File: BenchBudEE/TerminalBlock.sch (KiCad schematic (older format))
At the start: 2 parts, among them P4 12 pin terminal block, P5 3 Pin TB

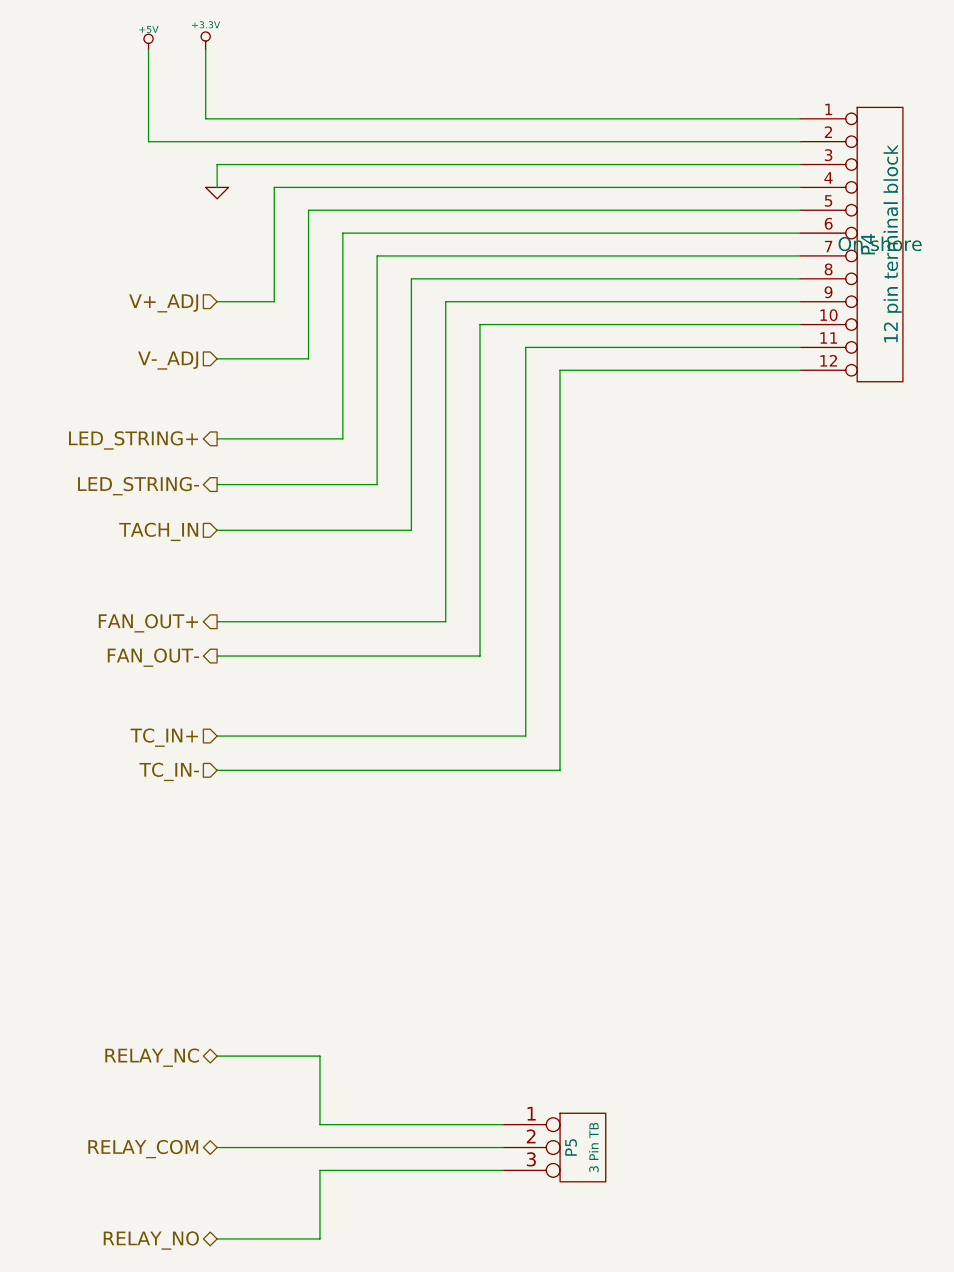
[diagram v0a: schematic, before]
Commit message: Ground and Power Planes
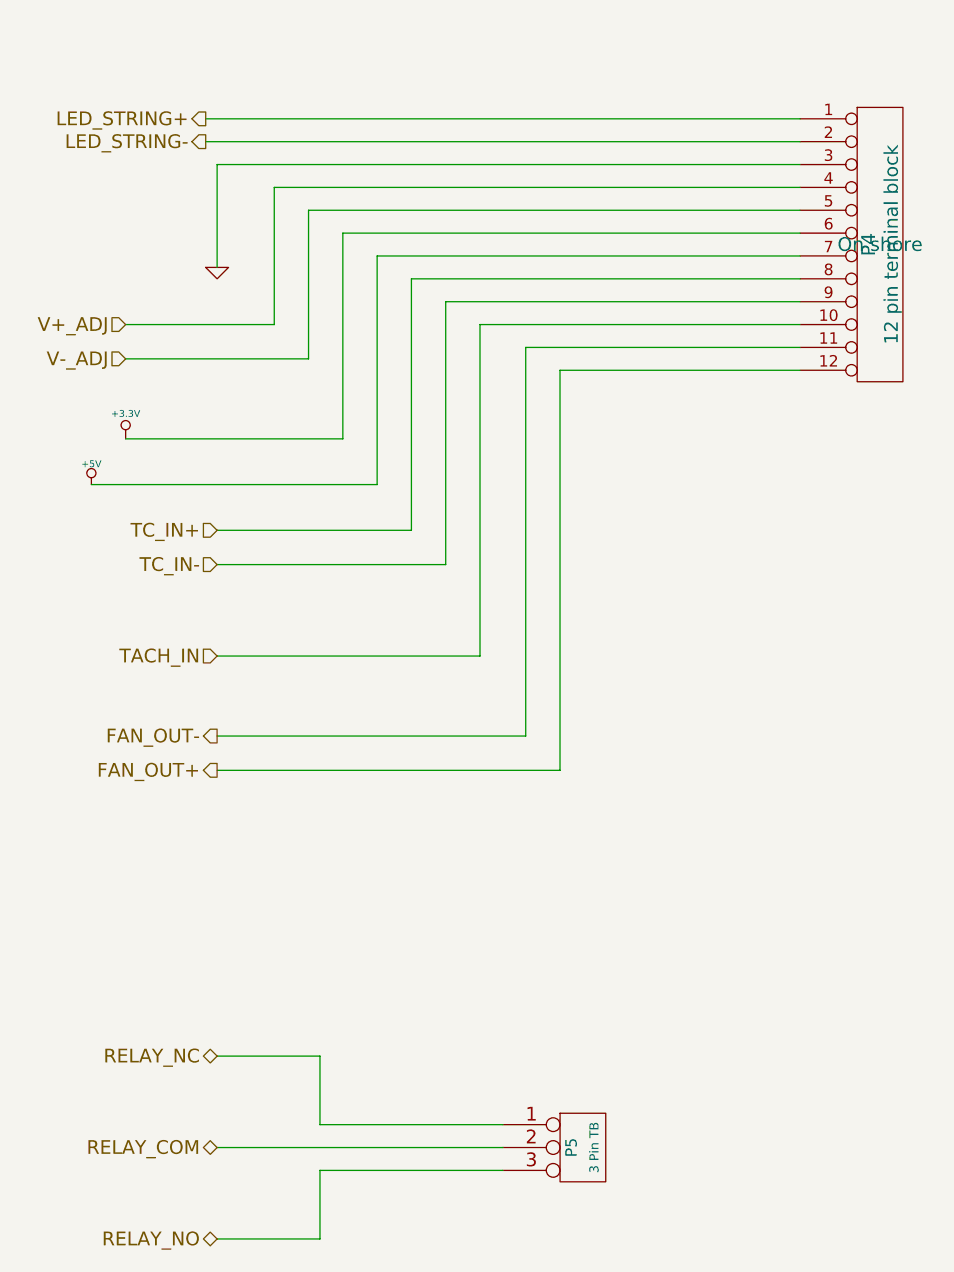
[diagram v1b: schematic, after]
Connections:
- net +3.3V: now also P4.6 (P6); no longer P4.1 (P1)
- net +5V: now also P4.7 (P7); no longer P4.2 (P2)
- net FAN_OUT+: now also P4.12 (P12); no longer P4.9 (P9)
- net FAN_OUT-: now also P4.11 (P11); no longer P4.10 (P10)
- net LED_STRING+: now also P4.1 (P1); no longer P4.6 (P6)
- net LED_STRING-: now also P4.2 (P2); no longer P4.7 (P7)
- net TACH_IN: now also P4.10 (P10); no longer P4.8 (P8)
- net TC_IN+: now also P4.8 (P8); no longer P4.11 (P11)
- net TC_IN-: now also P4.9 (P9); no longer P4.12 (P12)
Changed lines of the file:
@@
 Sheet 6 9
 Title ""
-Date "27 feb 2014"
+Date "1 mar 2014"
 Rev ""
 Comp ""
@@
 Comment4 ""
 $EndDescr
-Text HLabel 1850 1800 0    60   Input ~ 0
+Text HLabel 1450 1900 0    60   Input ~ 0
 V+_ADJ
-Text HLabel 1850 2050 0    60   Input ~ 0
+Text HLabel 1450 2050 0    60   Input ~ 0
 V-_ADJ
+Text HLabel 1850 3350 0    60   Input ~ 0
+TACH_IN
+Text HLabel 1800 1000 0    60   Output ~ 0
+LED_STRING+
+Text HLabel 1800 1100 0    60   Output ~ 0
+LED_STRING-
 Text HLabel 1850 2800 0    60   Input ~ 0
-TACH_IN
-Text HLabel 1850 2400 0    60   Output ~ 0
-LED_STRING+
-Text HLabel 1850 2600 0    60   Output ~ 0
-LED_STRING-
-Text HLabel 1850 3700 0    60   Input ~ 0
 TC_IN+
-Text HLabel 1850 3850 0    60   Input ~ 0
+Text HLabel 1850 2950 0    60   Input ~ 0
 TC_IN-
 Text HLabel 1850 5500 0    60   BiDi ~ 0
@@
 Text HLabel 1850 5900 0    60   BiDi ~ 0
 RELAY_NO
-Text HLabel 1850 3200 0    60   Output ~ 0
+Text HLabel 1850 3850 0    60   Output ~ 0
 FAN_OUT+
-Text HLabel 1850 3350 0    60   Output ~ 0
+Text HLabel 1850 3700 0    60   Output ~ 0
 FAN_OUT-
 $Comp
-L +3.3V #PWR038
+L +3.3V #PWR41
 U 1 1 52F7DDCB
-P 1800 700
-F 0 "#PWR038" H 1800 660 30  0001 C CNN
-F 1 "+3.3V" H 1800 810 30  0000 C CNN
-F 2 "" H 1800 700 60  0000 C CNN
-F 3 "" H 1800 700 60  0000 C CNN
-	1    1800 700
+P 1450 2400
+F 0 "#PWR41" H 1450 2360 30  0001 C CNN
+F 1 "+3.3V" H 1450 2510 30  0000 C CNN
+F 2 "" H 1450 2400 60  0000 C CNN
+F 3 "" H 1450 2400 60  0000 C CNN
+	1    1450 2400
 	1    0    0    -1
 $EndComp
 $Comp
-L +5V #PWR039
+L +5V #PWR40
 U 1 1 52F7DDDA
-P 1550 700
-F 0 "#PWR039" H 1550 790 20  0001 C CNN
-F 1 "+5V" H 1550 790 30  0000 C CNN
-F 2 "" H 1550 700 60  0000 C CNN
-F 3 "" H 1550 700 60  0000 C CNN
-	1    1550 700
+P 1300 2600
+F 0 "#PWR40" H 1300 2690 20  0001 C CNN
+F 1 "+5V" H 1300 2690 30  0000 C CNN
+F 2 "" H 1300 2600 60  0000 C CNN
+F 3 "" H 1300 2600 60  0000 C CNN
+	1    1300 2600
 	1    0    0    -1
 $EndComp
 $Comp
-L GND #PWR040
+L GND #PWR42
 U 1 1 52F7DDE9
-P 1850 1300
-F 0 "#PWR040" H 1850 1300 30  0001 C CNN
-F 1 "GND" H 1850 1230 30  0001 C CNN
-F 2 "" H 1850 1300 60  0000 C CNN
-F 3 "" H 1850 1300 60  0000 C CNN
-	1    1850 1300
+P 1850 1650
+F 0 "#PWR42" H 1850 1650 30  0001 C CNN
+F 1 "GND" H 1850 1580 30  0001 C CNN
+F 2 "" H 1850 1650 60  0000 C CNN
+F 3 "" H 1850 1650 60  0000 C CNN
+	1    1850 1650
 	1    0    0    -1
 $EndComp
@@
 	4400 1000 1800 1000
 Wire Wire Line
-	1800 1000 1800 700
+	1800 1100 4400 1100
 Wire Wire Line
-	1550 700  1550 1100
-Wire Wire Line
-	1550 1100 4400 1100
-Wire Wire Line
-	1850 1300 1850 1200
+	1850 1650 1850 1200
 Wire Wire Line
 	1850 1200 4400 1200
 Wire Wire Line
-	1850 1800 2100 1800
-Wire Wire Line
-	2100 1800 2100 1300
+	2100 1300 2100 1900
 Wire Wire Line
 	2100 1300 4400 1300
@@
 	2250 1400 2250 2050
 Wire Wire Line
-	2250 2050 1850 2050
-Wire Wire Line
-	1850 2400 2400 2400
+	1450 2400 2400 2400
 Wire Wire Line
 	2400 2400 2400 1500
@@
 	2550 1600 2550 2600
 Wire Wire Line
-	2550 2600 1850 2600
+	2550 2600 1300 2600
 Wire Wire Line
 	1850 2800 2700 2800
@@
 	2700 1700 4400 1700
 Wire Wire Line
-	1850 3200 2850 3200
-Wire Wire Line
-	2850 3200 2850 1800
+	2850 2950 2850 1800
 Wire Wire Line
 	2850 1800 4400 1800
@@
 Wire Wire Line
 	2300 5600 3100 5600
+Wire Wire Line
+	1850 2950 2850 2950
+Wire Wire Line
+	2100 1900 1450 1900
+Wire Wire Line
+	2250 2050 1450 2050
 $EndSCHEMATC

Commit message: Reality Check
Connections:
- net RELAY_NC: now also P5.3 (P3); no longer P5.1 (P1)
- net RELAY_NO: now also P5.1 (P1); no longer P5.3 (P3)
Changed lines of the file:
@@
 Text HLabel 1850 5500 0    60   BiDi ~ 0
 RELAY_COM
+Text HLabel 1850 5900 0    60   BiDi ~ 0
+RELAY_NC
 Text HLabel 1850 5100 0    60   BiDi ~ 0
-RELAY_NC
-Text HLabel 1850 5900 0    60   BiDi ~ 0
 RELAY_NO
 Text HLabel 1850 3850 0    60   Output ~ 0

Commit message: Layout Work Session 4
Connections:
- net +3.3V: now also P4.10 (P10); no longer P4.6 (P6)
- net +5V: now also P4.9 (P9); no longer P4.7 (P7)
- net FAN_OUT+: now also P4.5 (P5); no longer P4.12 (P12)
- net FAN_OUT-: now also P4.4 (P4); no longer P4.11 (P11)
- net GND: now also P4.8 (P8); no longer P4.3 (P3)
- net TACH_IN: now also P4.3 (P3); no longer P4.10 (P10)
- net TC_IN+: now also P4.7 (P7); no longer P4.8 (P8)
- net TC_IN-: now also P4.6 (P6); no longer P4.9 (P9)
- net V+_ADJ: now also P4.12 (P12); no longer P4.4 (P4)
- net V-_ADJ: now also P4.11 (P11); no longer P4.5 (P5)
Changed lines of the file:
@@
 Sheet 6 9
 Title ""
-Date "1 mar 2014"
+Date "2 mar 2014"
 Rev ""
 Comp ""
@@
 Comment4 ""
 $EndDescr
-Text HLabel 1450 1900 0    60   Input ~ 0
+Text HLabel 1850 3850 0    60   Input ~ 0
 V+_ADJ
-Text HLabel 1450 2050 0    60   Input ~ 0
+Text HLabel 1850 3700 0    60   Input ~ 0
 V-_ADJ
-Text HLabel 1850 3350 0    60   Input ~ 0
+Text HLabel 1850 1650 0    60   Input ~ 0
 TACH_IN
-Text HLabel 1800 1000 0    60   Output ~ 0
+Text HLabel 1850 1000 0    60   Output ~ 0
 LED_STRING+
-Text HLabel 1800 1100 0    60   Output ~ 0
+Text HLabel 1850 1100 0    60   Output ~ 0
 LED_STRING-
-Text HLabel 1850 2800 0    60   Input ~ 0
+Text HLabel 1850 2450 0    60   Input ~ 0
 TC_IN+
-Text HLabel 1850 2950 0    60   Input ~ 0
+Text HLabel 1850 2300 0    60   Input ~ 0
 TC_IN-
 Text HLabel 1850 5500 0    60   BiDi ~ 0
@@
 Text HLabel 1850 5100 0    60   BiDi ~ 0
 RELAY_NO
-Text HLabel 1850 3850 0    60   Output ~ 0
+Text HLabel 1850 2050 0    60   Output ~ 0
 FAN_OUT+
-Text HLabel 1850 3700 0    60   Output ~ 0
+Text HLabel 1850 1850 0    60   Output ~ 0
 FAN_OUT-
 $Comp
 L +3.3V #PWR034
 U 1 1 52F7DDCB
-P 1450 2400
-F 0 "#PWR034" H 1450 2360 30  0001 C CNN
-F 1 "+3.3V" H 1450 2510 30  0000 C CNN
-F 2 "" H 1450 2400 60  0000 C CNN
-F 3 "" H 1450 2400 60  0000 C CNN
-	1    1450 2400
+P 1400 3300
+F 0 "#PWR034" H 1400 3260 30  0001 C CNN
+F 1 "+3.3V" H 1400 3410 30  0000 C CNN
+F 2 "" H 1400 3300 60  0000 C CNN
+F 3 "" H 1400 3300 60  0000 C CNN
+	1    1400 3300
 	1    0    0    -1
 $EndComp
@@
 L +5V #PWR035
 U 1 1 52F7DDDA
-P 1300 2600
-F 0 "#PWR035" H 1300 2690 20  0001 C CNN
-F 1 "+5V" H 1300 2690 30  0000 C CNN
-F 2 "" H 1300 2600 60  0000 C CNN
-F 3 "" H 1300 2600 60  0000 C CNN
-	1    1300 2600
+P 1550 3050
+F 0 "#PWR035" H 1550 3140 20  0001 C CNN
+F 1 "+5V" H 1550 3140 30  0000 C CNN
+F 2 "" H 1550 3050 60  0000 C CNN
+F 3 "" H 1550 3050 60  0000 C CNN
+	1    1550 3050
 	1    0    0    -1
 $EndComp
@@
 L GND #PWR036
 U 1 1 52F7DDE9
-P 1850 1650
-F 0 "#PWR036" H 1850 1650 30  0001 C CNN
-F 1 "GND" H 1850 1580 30  0001 C CNN
-F 2 "" H 1850 1650 60  0000 C CNN
-F 3 "" H 1850 1650 60  0000 C CNN
-	1    1850 1650
+P 1850 2800
+F 0 "#PWR036" H 1850 2800 30  0001 C CNN
+F 1 "GND" H 1850 2730 30  0001 C CNN
+F 2 "" H 1850 2800 60  0000 C CNN
+F 3 "" H 1850 2800 60  0000 C CNN
+	1    1850 2800
 	1    0    0    -1
 $EndComp
@@
 $EndComp
 Wire Wire Line
-	4400 1000 1800 1000
+	4400 1000 1850 1000
 Wire Wire Line
-	1800 1100 4400 1100
+	1850 1100 4400 1100
 Wire Wire Line
-	1850 1650 1850 1200
+	1950 1200 4400 1200
 Wire Wire Line
-	1850 1200 4400 1200
-Wire Wire Line
-	2100 1300 2100 1900
+	2100 1300 2100 1850
 Wire Wire Line
 	2100 1300 4400 1300
@@
 	2250 1400 2250 2050
 Wire Wire Line
-	1450 2400 2400 2400
+	1850 2300 2400 2300
 Wire Wire Line
-	2400 2400 2400 1500
+	2400 2300 2400 1500
 Wire Wire Line
 	2400 1500 4400 1500
@@
 	4400 1600 2550 1600
 Wire Wire Line
-	2550 1600 2550 2600
+	2550 1600 2550 2450
 Wire Wire Line
-	2550 2600 1300 2600
+	2550 2450 1850 2450
 Wire Wire Line
-	1850 2800 2700 2800
+	1850 2650 2700 2650
 Wire Wire Line
-	2700 2800 2700 1700
+	2700 2650 2700 1700
 Wire Wire Line
 	2700 1700 4400 1700
 Wire Wire Line
-	2850 2950 2850 1800
+	2850 3100 2850 1800
 Wire Wire Line
 	2850 1800 4400 1800
@@
 	3000 1900 4400 1900
 Wire Wire Line
-	3000 1900 3000 3350
+	3000 3350 3000 1900
 Wire Wire Line
-	3000 3350 1850 3350
+	1400 3350 3000 3350
 Wire Wire Line
 	1850 3700 3200 3700
@@
 	2300 5600 3100 5600
 Wire Wire Line
-	1850 2950 2850 2950
+	1550 3100 2850 3100
 Wire Wire Line
-	2100 1900 1450 1900
+	2100 1850 1850 1850
 Wire Wire Line
-	2250 2050 1450 2050
+	2250 2050 1850 2050
+Wire Wire Line
+	1400 3300 1400 3350
+Wire Wire Line
+	1550 3100 1550 3050
+Wire Wire Line
+	1950 1200 1950 1650
+Wire Wire Line
+	1950 1650 1850 1650
+Wire Wire Line
+	1850 2650 1850 2800
 $EndSCHEMATC

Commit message: Layout Work Session 5
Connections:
- net GND renamed GND_PWR
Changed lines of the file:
@@
 FAN_OUT-
 $Comp
-L +3.3V #PWR034
+L +3.3V #PWR035
 U 1 1 52F7DDCB
 P 1400 3300
-F 0 "#PWR034" H 1400 3260 30  0001 C CNN
+F 0 "#PWR035" H 1400 3260 30  0001 C CNN
 F 1 "+3.3V" H 1400 3410 30  0000 C CNN
 F 2 "" H 1400 3300 60  0000 C CNN
@@
 $EndComp
 $Comp
-L +5V #PWR035
+L +5V #PWR036
 U 1 1 52F7DDDA
 P 1550 3050
-F 0 "#PWR035" H 1550 3140 20  0001 C CNN
+F 0 "#PWR036" H 1550 3140 20  0001 C CNN
 F 1 "+5V" H 1550 3140 30  0000 C CNN
 F 2 "" H 1550 3050 60  0000 C CNN
 F 3 "" H 1550 3050 60  0000 C CNN
 	1    1550 3050
-	1    0    0    -1
-$EndComp
-$Comp
-L GND #PWR036
-U 1 1 52F7DDE9
-P 1850 2800
-F 0 "#PWR036" H 1850 2800 30  0001 C CNN
-F 1 "GND" H 1850 2730 30  0001 C CNN
-F 2 "" H 1850 2800 60  0000 C CNN
-F 3 "" H 1850 2800 60  0000 C CNN
-	1    1850 2800
 	1    0    0    -1
 $EndComp
@@
 Wire Wire Line
 	1850 2650 1850 2800
+$Comp
+L GND_PWR #PWR037
+U 1 1 53137D5D
+P 1850 2800
+F 0 "#PWR037" H 1850 2800 30  0001 C CNN
+F 1 "GND_PWR" H 1850 2730 30  0000 C CNN
+F 2 "" H 1850 2800 60  0000 C CNN
+F 3 "" H 1850 2800 60  0000 C CNN
+	1    1850 2800
+	1    0    0    -1
+$EndComp
 $EndSCHEMATC

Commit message: Layout Work Session 6
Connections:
- net +5V: now also P4.8 (P8); no longer P4.9 (P9)
- net GND_PWR: now also P4.9 (P9); no longer P4.8 (P8)
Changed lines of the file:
@@
 Sheet 6 9
 Title ""
-Date "2 mar 2014"
+Date "3 mar 2014"
 Rev ""
 Comp ""
@@
 FAN_OUT-
 $Comp
-L +3.3V #PWR035
+L +3.3V #PWR46
 U 1 1 52F7DDCB
 P 1400 3300
-F 0 "#PWR035" H 1400 3260 30  0001 C CNN
+F 0 "#PWR46" H 1400 3260 30  0001 C CNN
 F 1 "+3.3V" H 1400 3410 30  0000 C CNN
 F 2 "" H 1400 3300 60  0000 C CNN
@@
 $EndComp
 $Comp
-L +5V #PWR036
+L +5V #PWR47
 U 1 1 52F7DDDA
-P 1550 3050
-F 0 "#PWR036" H 1550 3140 20  0001 C CNN
-F 1 "+5V" H 1550 3140 30  0000 C CNN
-F 2 "" H 1550 3050 60  0000 C CNN
-F 3 "" H 1550 3050 60  0000 C CNN
-	1    1550 3050
+P 1850 2800
+F 0 "#PWR47" H 1850 2890 20  0001 C CNN
+F 1 "+5V" H 1850 2890 30  0000 C CNN
+F 2 "" H 1850 2800 60  0000 C CNN
+F 3 "" H 1850 2800 60  0000 C CNN
+	1    1850 2800
 	1    0    0    -1
 $EndComp
@@
 	2550 2450 1850 2450
 Wire Wire Line
-	1850 2650 2700 2650
+	1850 2850 2700 2850
 Wire Wire Line
-	2700 2650 2700 1700
+	2700 2850 2700 1700
 Wire Wire Line
 	2700 1700 4400 1700
-Wire Wire Line
-	2850 3100 2850 1800
 Wire Wire Line
 	2850 1800 4400 1800
@@
 	2300 5600 3100 5600
 Wire Wire Line
-	1550 3100 2850 3100
-Wire Wire Line
 	2100 1850 1850 1850
 Wire Wire Line
@@
 	1400 3300 1400 3350
 Wire Wire Line
-	1550 3100 1550 3050
-Wire Wire Line
 	1950 1200 1950 1650
 Wire Wire Line
 	1950 1650 1850 1650
 Wire Wire Line
-	1850 2650 1850 2800
+	1850 2850 1850 2800
 $Comp
-L GND_PWR #PWR037
+L GND_PWR #PWR48
 U 1 1 53137D5D
-P 1850 2800
-F 0 "#PWR037" H 1850 2800 30  0001 C CNN
-F 1 "GND_PWR" H 1850 2730 30  0000 C CNN
-F 2 "" H 1850 2800 60  0000 C CNN
-F 3 "" H 1850 2800 60  0000 C CNN
-	1    1850 2800
+P 1700 3050
+F 0 "#PWR48" H 1700 3050 30  0001 C CNN
+F 1 "GND_PWR" H 1700 2980 30  0000 C CNN
+F 2 "" H 1700 3050 60  0000 C CNN
+F 3 "" H 1700 3050 60  0000 C CNN
+	1    1700 3050
 	1    0    0    -1
 $EndComp
+Wire Wire Line
+	1700 3050 1700 3000
+Wire Wire Line
+	1700 3000 2850 3000
+Wire Wire Line
+	2850 3000 2850 3000
+Wire Wire Line
+	2850 3000 2850 1800
 $EndSCHEMATC

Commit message: Layout Work Session 7
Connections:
- net +5V renamed +5P
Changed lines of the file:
@@
 FAN_OUT-
 $Comp
-L +3.3V #PWR040
+L +3.3V #PWR46
 U 1 1 52F7DDCB
 P 1400 3300
-F 0 "#PWR040" H 1400 3260 30  0001 C CNN
+F 0 "#PWR46" H 1400 3260 30  0001 C CNN
 F 1 "+3.3V" H 1400 3410 30  0000 C CNN
 F 2 "" H 1400 3300 60  0000 C CNN
 F 3 "" H 1400 3300 60  0000 C CNN
 	1    1400 3300
-	1    0    0    -1
-$EndComp
-$Comp
-L +5V #PWR041
-U 1 1 52F7DDDA
-P 1850 2800
-F 0 "#PWR041" H 1850 2890 20  0001 C CNN
-F 1 "+5V" H 1850 2890 30  0000 C CNN
-F 2 "" H 1850 2800 60  0000 C CNN
-F 3 "" H 1850 2800 60  0000 C CNN
-	1    1850 2800
 	1    0    0    -1
 $EndComp
@@
 	1850 2850 1850 2800
 $Comp
-L GND_PWR #PWR042
+L GND_PWR #PWR47
 U 1 1 53137D5D
 P 1700 3050
-F 0 "#PWR042" H 1700 3050 30  0001 C CNN
+F 0 "#PWR47" H 1700 3050 30  0001 C CNN
 F 1 "GND_PWR" H 1700 2980 30  0000 C CNN
 F 2 "" H 1700 3050 60  0000 C CNN
@@
 Wire Wire Line
 	2850 3000 2850 1800
+$Comp
+L +5P #PWR48
+U 1 1 5314DD8C
+P 1850 2800
+F 0 "#PWR48" H 1850 2930 20  0001 C CNN
+F 1 "+5P" H 1850 2900 30  0000 C CNN
+F 2 "~" H 1850 2800 60  0000 C CNN
+F 3 "~" H 1850 2800 60  0000 C CNN
+	1    1850 2800
+	1    0    0    -1
+$EndComp
 $EndSCHEMATC
